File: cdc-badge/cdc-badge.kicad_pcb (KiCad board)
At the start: 4 copper layers, 85 x 110 mm, 158 parts, among them J1 USB_C, J2 JST S2B-PH-SM4-TB, J3 Conn_02x20_Odd_Even, J4 Conn_Grove, J5 Conn_02x03_Odd_Even, J6 Conn_01x06, J7 Conn_01x24, Q1 Si1308EDL, Q2 Si1308EDL, SW0 0, SW1 1, SW10 YES, SW11 NO, SW12 power on/reset, SW13 reset, SW14 flash/power off, SW15 MST-22D18G2 3J, SW16 MST-22D18G2 3J, SW2 2, SW3 3, SW4 4, SW5 5, SW6 6, SW7 7, SW8 8, SW9 9, U1 ESP32-S3-WROOM-1-N16R8, U2 TCA9535PWR, U3 TR01-C2P-T301, U5 TLV61070ADBVR, U6 BQ25895RTW, U8 TLV62569DBV

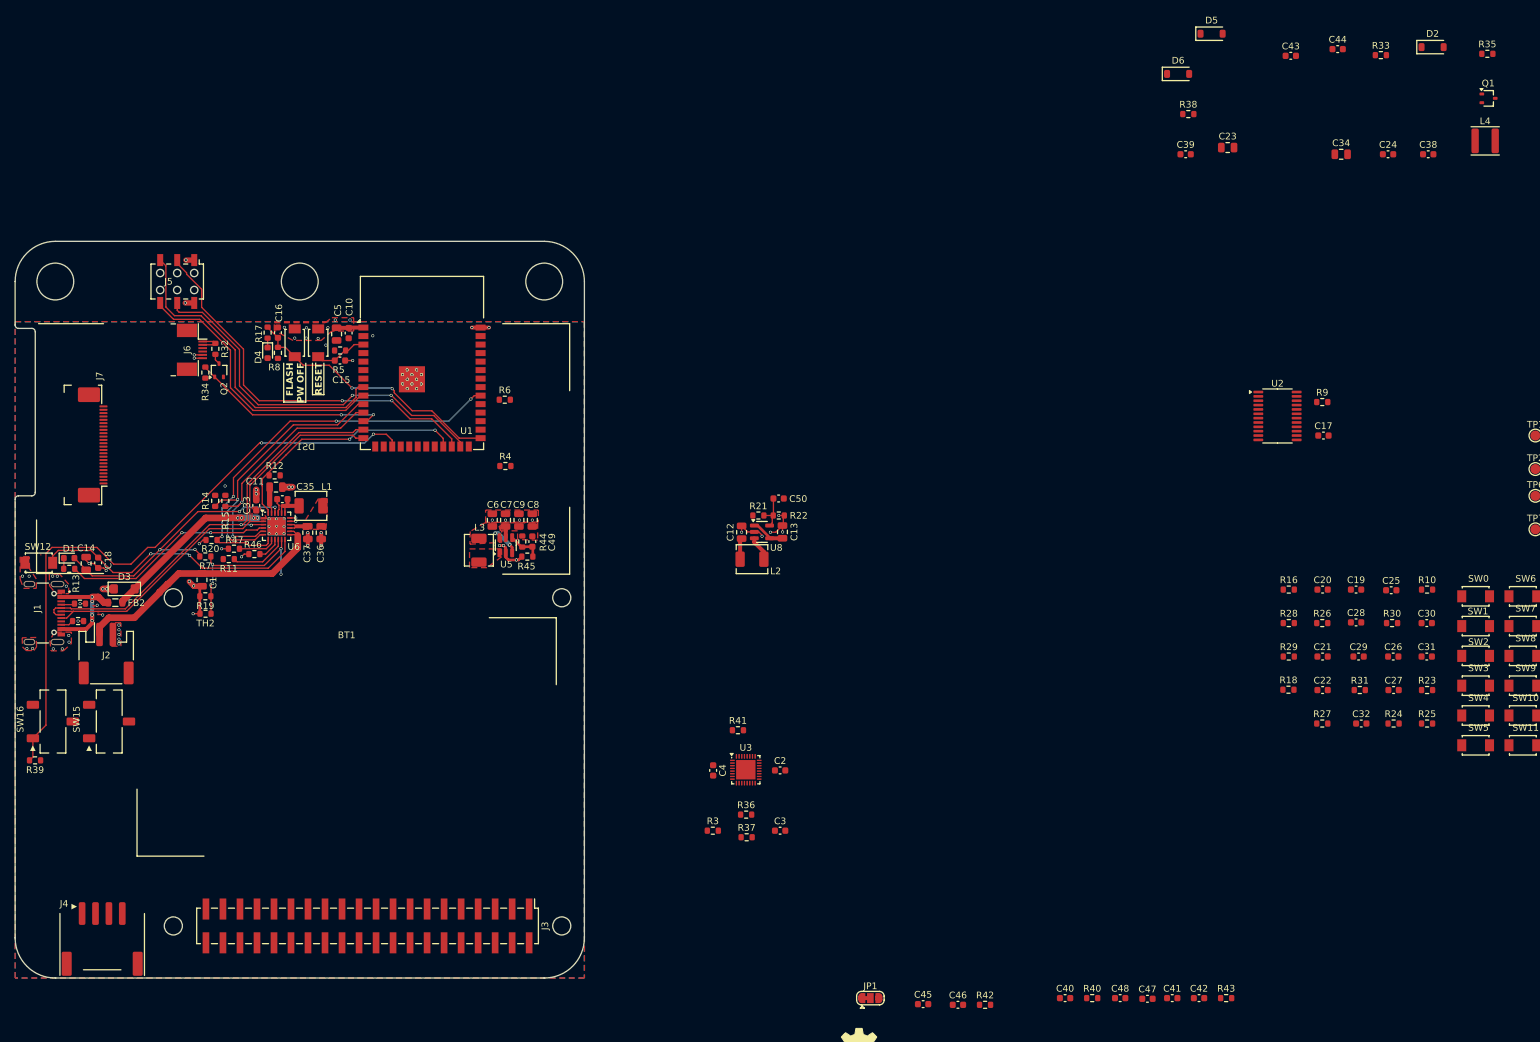
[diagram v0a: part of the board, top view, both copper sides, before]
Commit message: PCB/FP: Adjusted FPs for Display and Battery
Edited the user generated FPs, as EDC indicated warnings there:
Ref texts had to thin line thickness for silkscreen,
positions of REF values adjusted to final PCB appearance
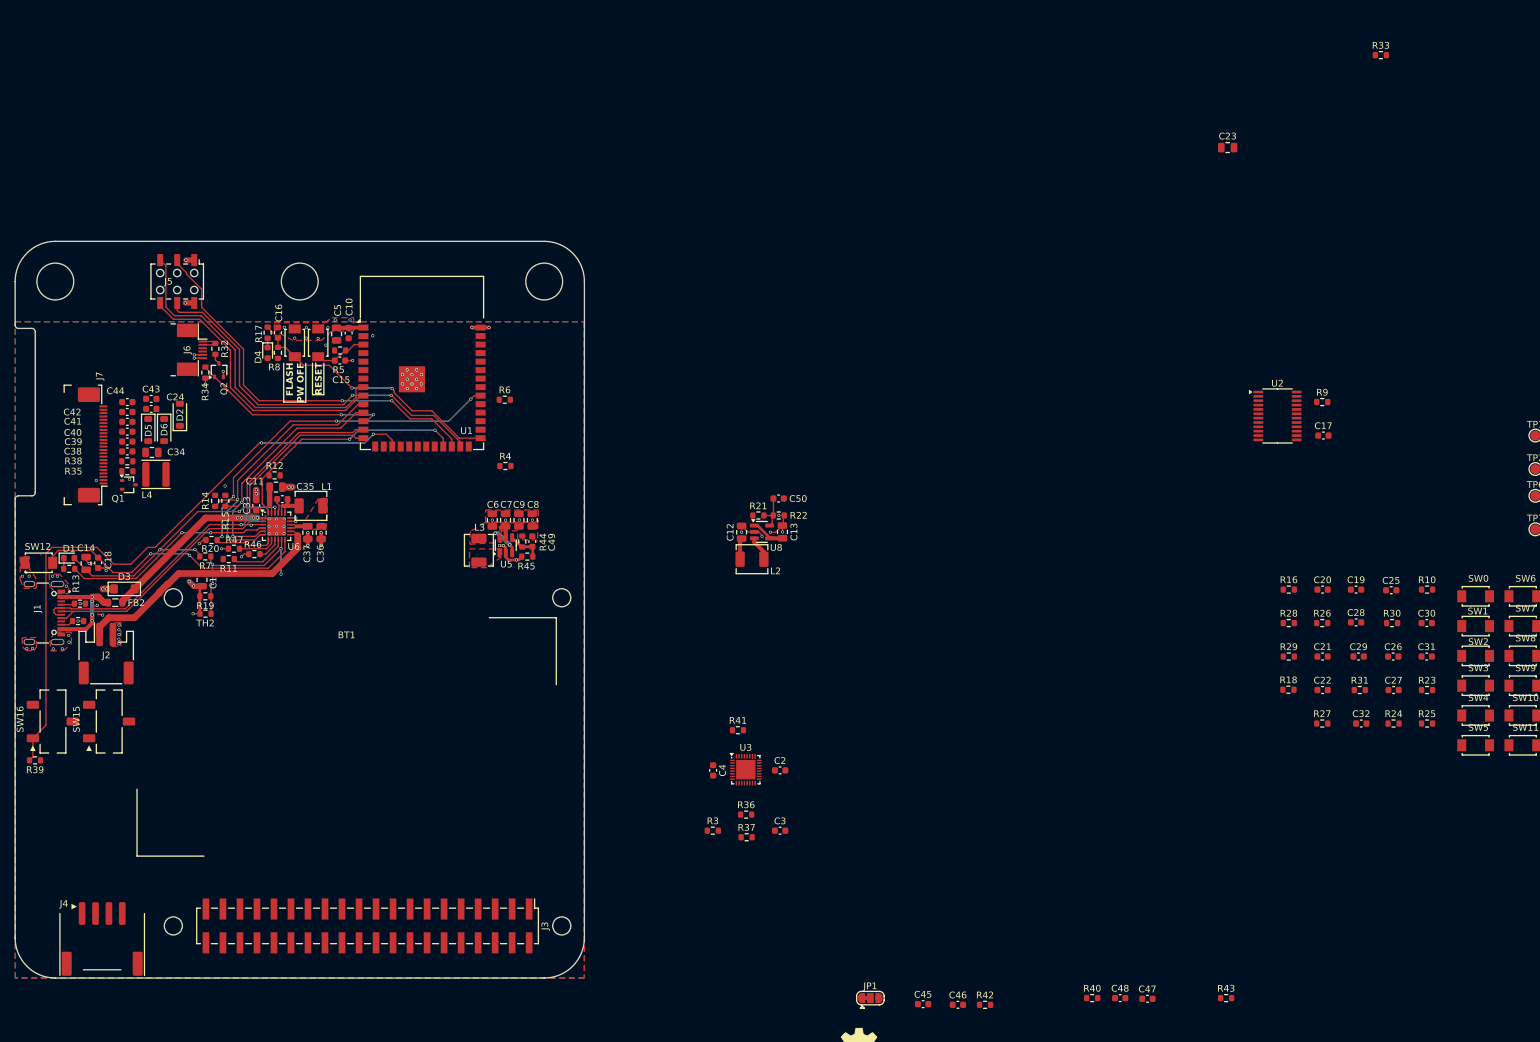
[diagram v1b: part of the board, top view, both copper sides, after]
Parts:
- moved R35 212.4 mm to (71.8, 83.3)
- moved Q1 211.1 mm to (72.0, 85.4)
- moved L4 204.6 mm to (76.0, 83.8)
- moved C38 199.3 mm to (71.8, 80.4)
- moved D2 194.9 mm to (79.6, 74.9), turned to 90 degrees
- moved C24 188.5 mm to (75.3, 74.0), turned to 180 degrees
- moved C44 188.3 mm to (71.8, 73.0)
- moved C34 183.1 mm to (75.4, 80.5), turned to 180 degrees
- moved C42 182.4 mm to (71.8, 74.5)
- moved C41 178.2 mm to (71.8, 76.0), turned to 180 degrees
- moved C43 177.7 mm to (75.3, 72.5)
- moved D5 169.4 mm to (74.9, 77.2), turned to -90 degrees
- moved R38 166.7 mm to (71.8, 81.8)
- moved C39 163.7 mm to (71.8, 78.9)
- moved C40 163.6 mm to (71.8, 77.4), turned to 180 degrees
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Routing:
- net GND: track 52.0 -> 53.7 mm, vias 64 -> 68

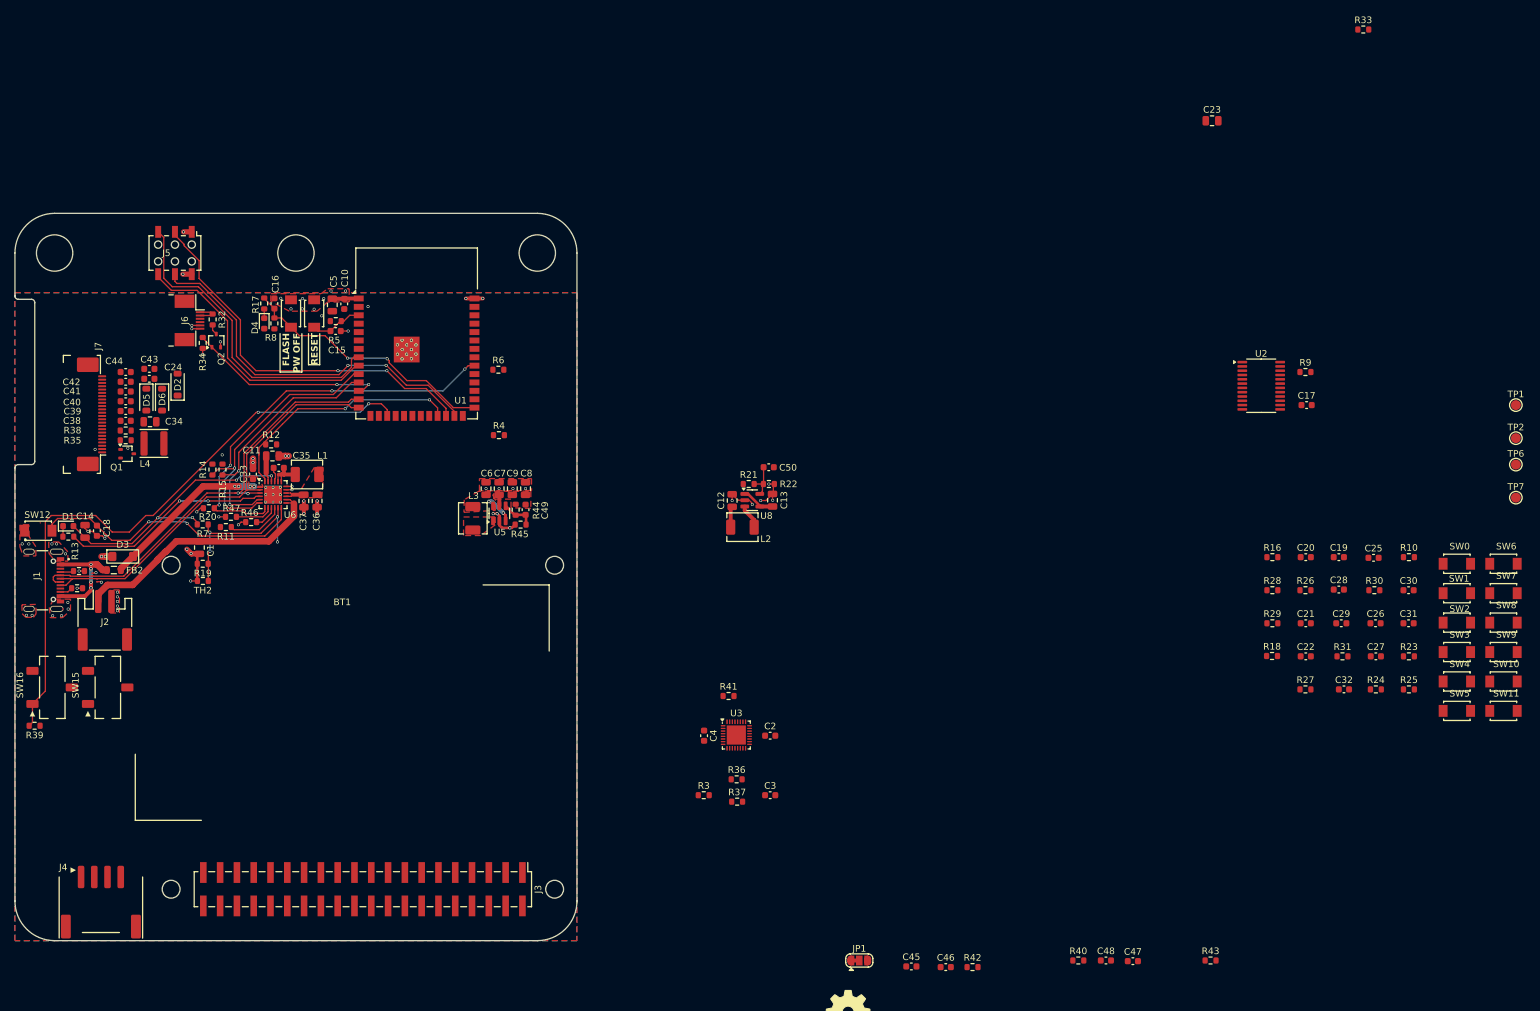
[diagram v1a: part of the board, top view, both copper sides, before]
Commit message: PCB: zones extended, rerouting and placement of critical components
-expanded zones/pours to the SAO connector region
-placed caps to to switches, SAO, Grove and display region
-(re)routing SPI connections between S3 and display connector
-finish replacement/arrangement of display components
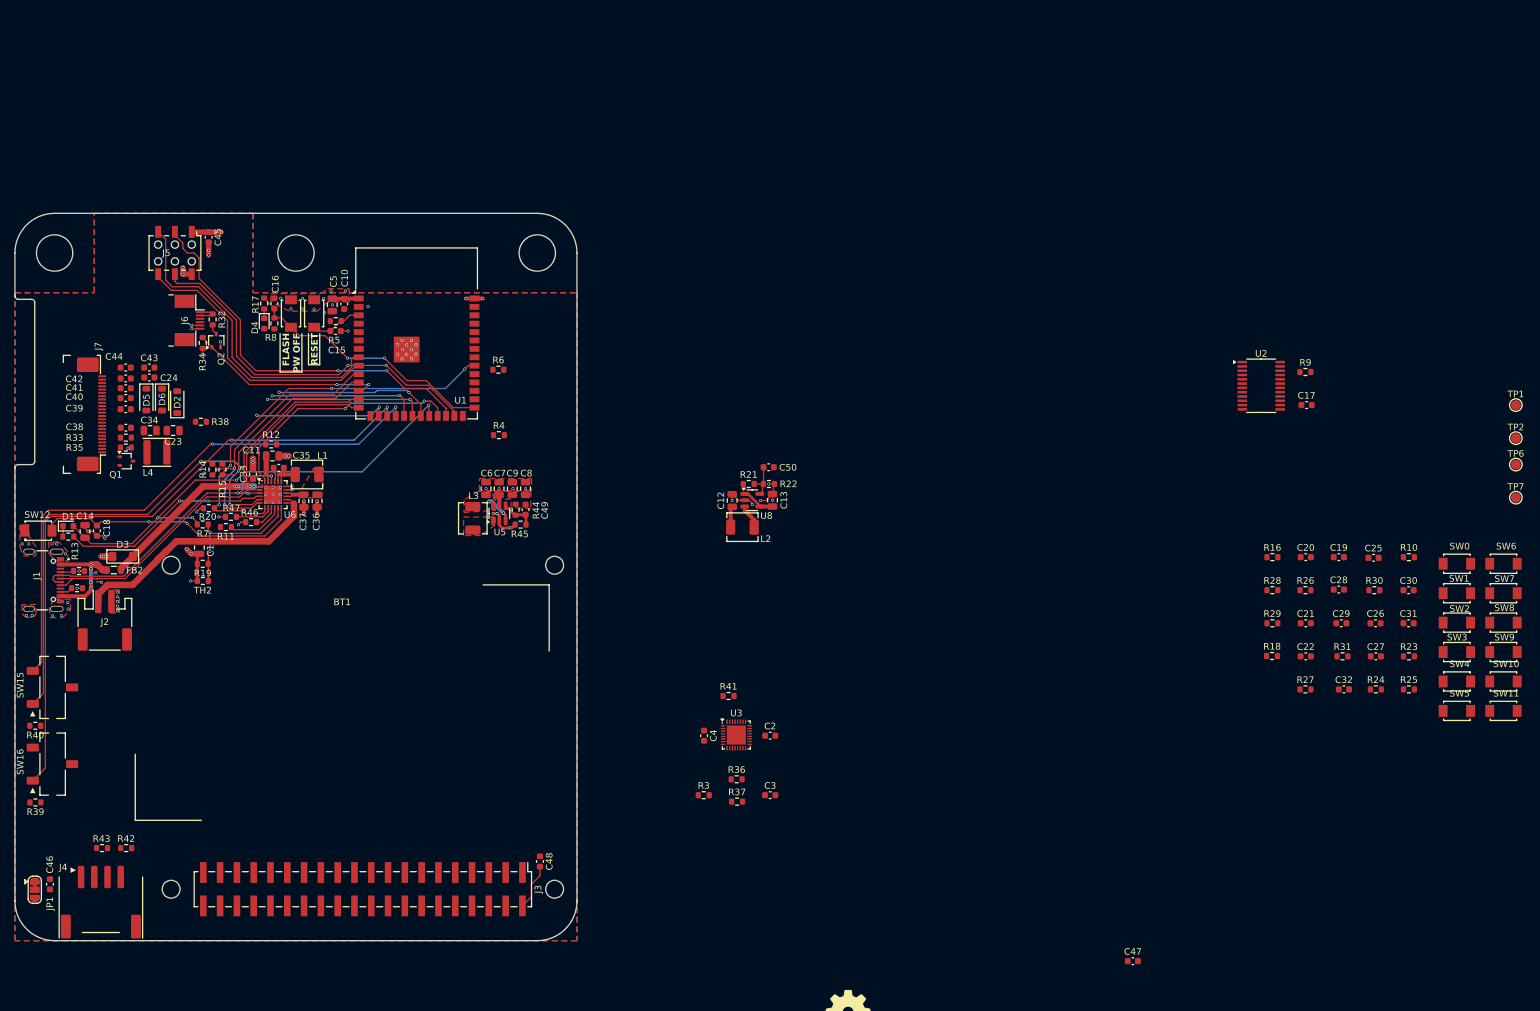
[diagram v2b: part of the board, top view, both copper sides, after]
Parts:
- moved R33 197.1 mm to (71.8, 82.9)
- moved R43 168.5 mm to (68.2, 145.0), turned to 180 degrees
- moved C23 164.0 mm to (78.9, 81.8), turned to 180 degrees
- moved R40 161.7 mm to (58.1, 126.5), turned to 180 degrees
- moved C45 153.2 mm to (84.3, 52.6), turned to -90 degrees
- moved C46 136.1 mm to (60.3, 150.5), turned to -90 degrees
- moved R42 129.3 mm to (71.8, 145.0)
- moved JP1 125.2 mm to (58.0, 151.3), turned to -90 degrees
- moved C48 86.9 mm to (134.4, 147.0), turned to -90 degrees
- moved R39 11.6 mm to (58.1, 138.1)
- moved SW16 11.6 mm to (60.7, 132.3)
- moved R38 11.5 mm to (83.1, 80.5)
- moved SW15 8.35 mm to (60.7, 120.7)
- moved D2 2.65 mm to (79.5, 77.5)
- moved L4 1.42 mm to (76.5, 85.2)
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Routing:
- net /SPI_CS1: track 0.00 -> 96.9 mm, vias 0 -> 2
- net /SPI_CS_TR01: track 0.00 -> 85.6 mm, vias 0 -> 2
- net /SPI_MOSI: track 0.00 -> 24.2 mm, vias 0 -> 2
- net /SPI_SCLK: track 0.00 -> 24.2 mm, vias 0 -> 2
- net /SPI_MISO: track 0.00 -> 22.7 mm, vias 0 -> 2
- net /SPI_RST_EPD: track 0.00 -> 20.5 mm, vias 0 -> 2
- net +5V: track 1.68 -> 8.72 mm
- net /SPI_CS0: track 94.4 -> 100.2 mm
- net Net-(U6-TS): track 25.3 -> 21.5 mm, vias 4 -> 2
- net +3.3V: track 8.14 -> 11.4 mm, vias 7 -> 9
- net GND: track 53.7 -> 56.6 mm, vias 68 -> 70
- net Net-(U6-~{QON}): track 42.3 -> 40.4 mm
- net /I2C1_SDA: track 58.3 -> 58.9 mm
